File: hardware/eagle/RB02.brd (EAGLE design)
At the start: 50 x 50 mm, 20 parts, among them J1 CON_TERMINAL_BLOCK_02-5MM, J2 CON_TERMINAL_BLOCK_02-5MM, J3 CON_TERMINAL_BLOCK_02-5MM, J4 CON_TERMINAL_BLOCK_02-5MM, K1 JS-M1A-12V-5, K2 JS-M1A-12V-5, Q1 BC337, Q2 BC337

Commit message: tweak gerbers
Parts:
- moved U$2 18.7 mm to (27.5, 25.0), turned to 90 degrees

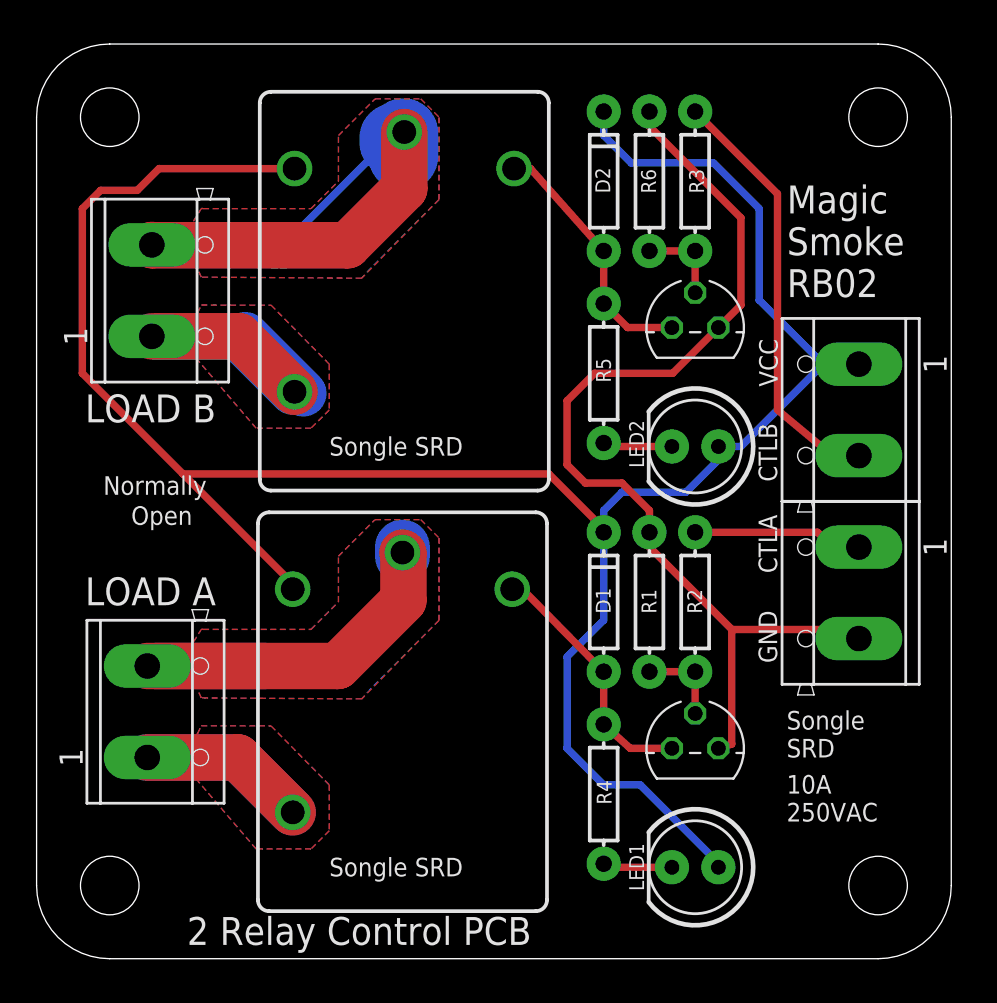
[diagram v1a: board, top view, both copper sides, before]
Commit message: JS-M1 relay package
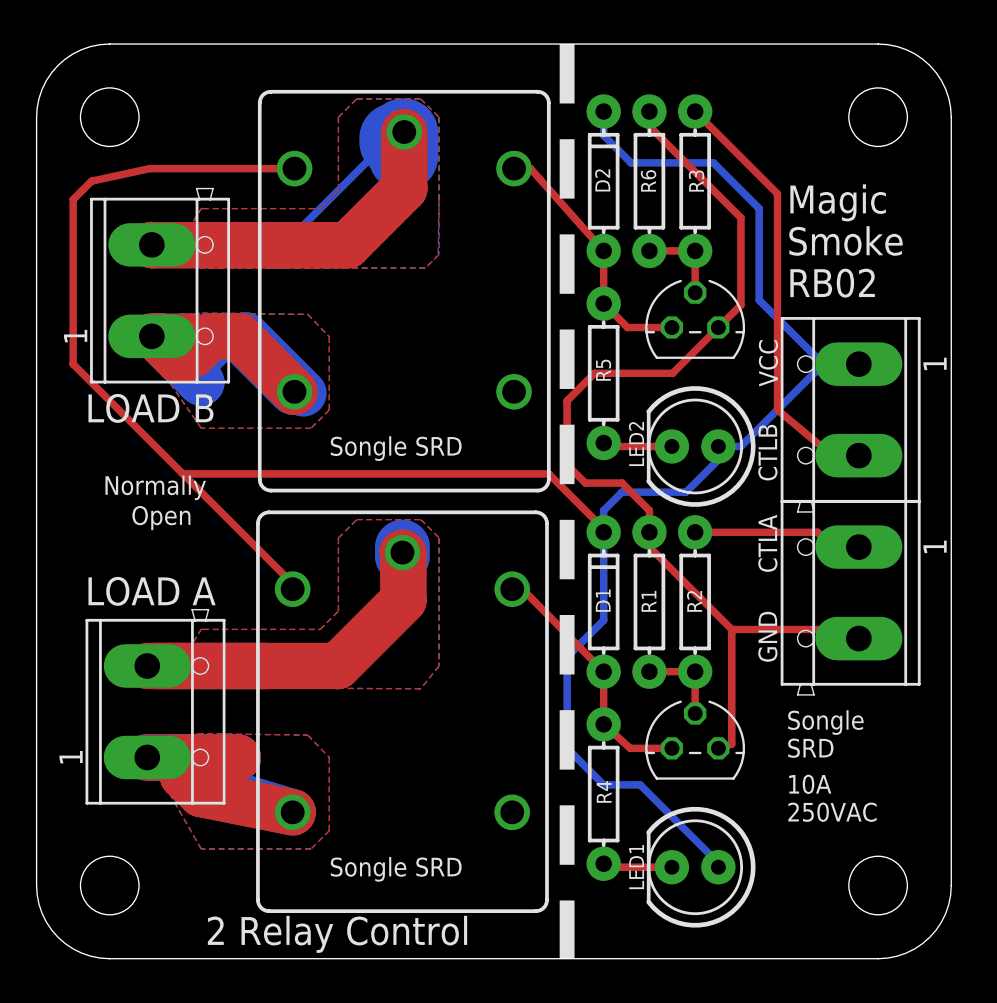
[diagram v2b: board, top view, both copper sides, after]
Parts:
- K1, K2: value JS-M1A-12V-5 -> JS-M1-12V-5; device relay:JS-M1A -> relay:JS-M
- moved U$2 20.4 mm to (20.0, 6.00), turned to 0 degrees
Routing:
- net LOAD_B1: track 26.3 -> 39.4 mm
- net LOAD_A1: track 18.4 -> 28.7 mm
- net VCC: track 126.6 -> 127.4 mm
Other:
- board text added: "2 Relay Control"
- board text added: "DANGER"
- board text added: "HIGH VOLTAGE"
- board text removed: "2 Relay Control PCB"
